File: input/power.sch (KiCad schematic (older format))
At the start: 59 parts, among them Q2 2STD1665T4, Q3 NSS1C300ET4G, U4 OPA830, U6 OPA830, U7 MCP1755S-3302E/DB, U8 NCP1117STAT3G

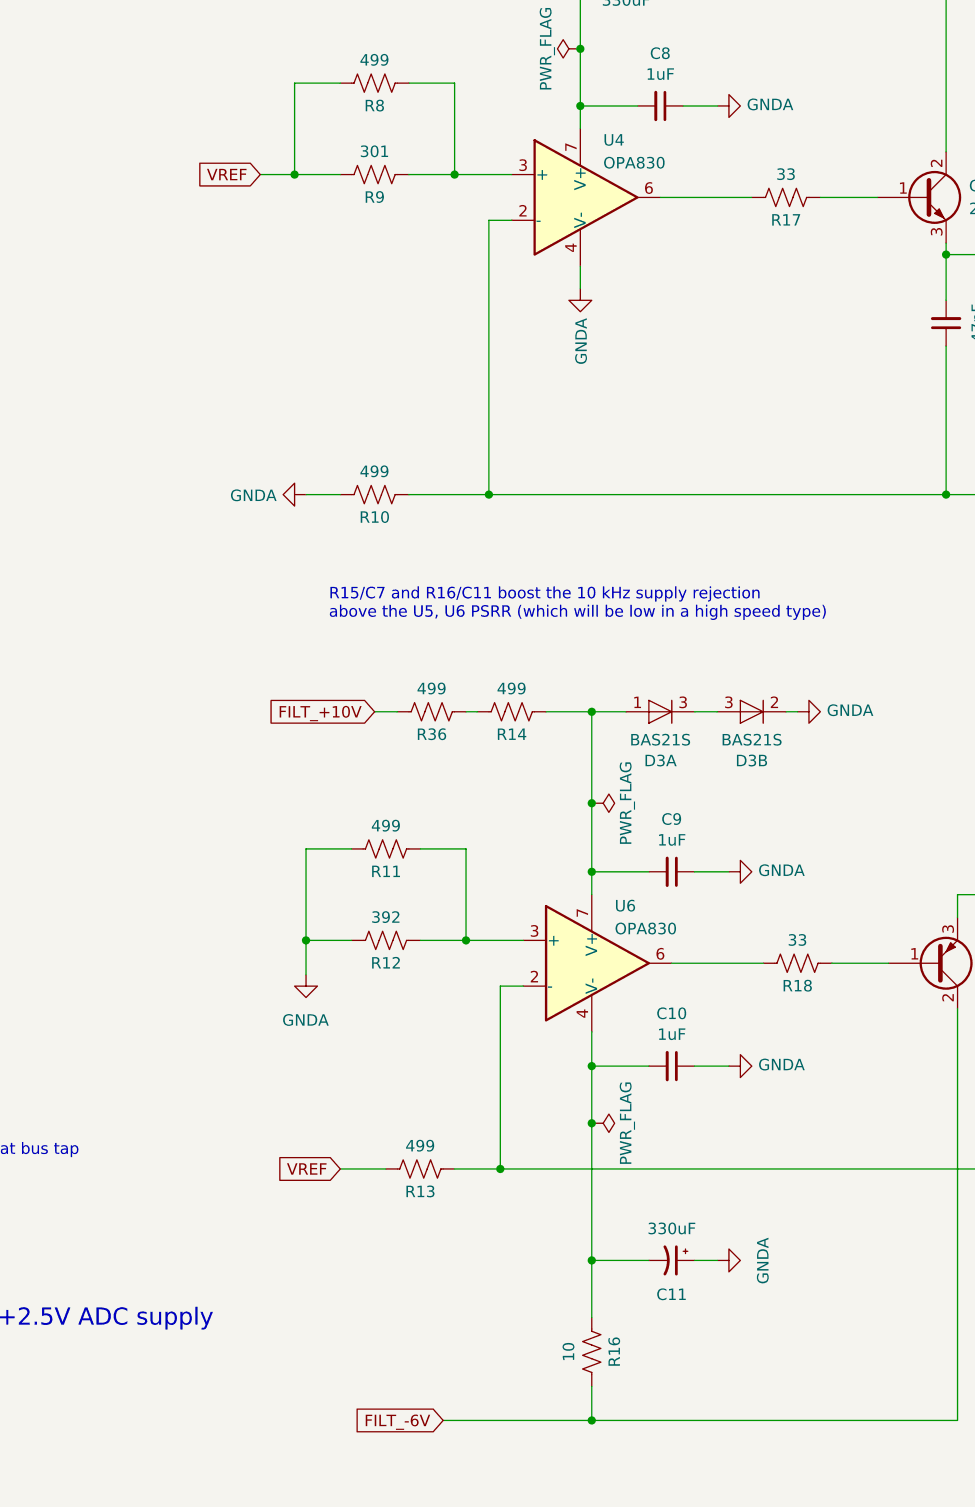
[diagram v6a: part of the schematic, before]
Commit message: Minor tweaks to schematic, and ongoing progress on PCB layout.
Changed BIST buffer to run off of CHAN1_V+, not the global V+.  This caused the CHAN_V+ net name to change.
On power.sch, added bypass caps for the VREF inputs to the V+/V- regulators.  Also, the BIST input lines now
have an RC filter, not just a resistor.
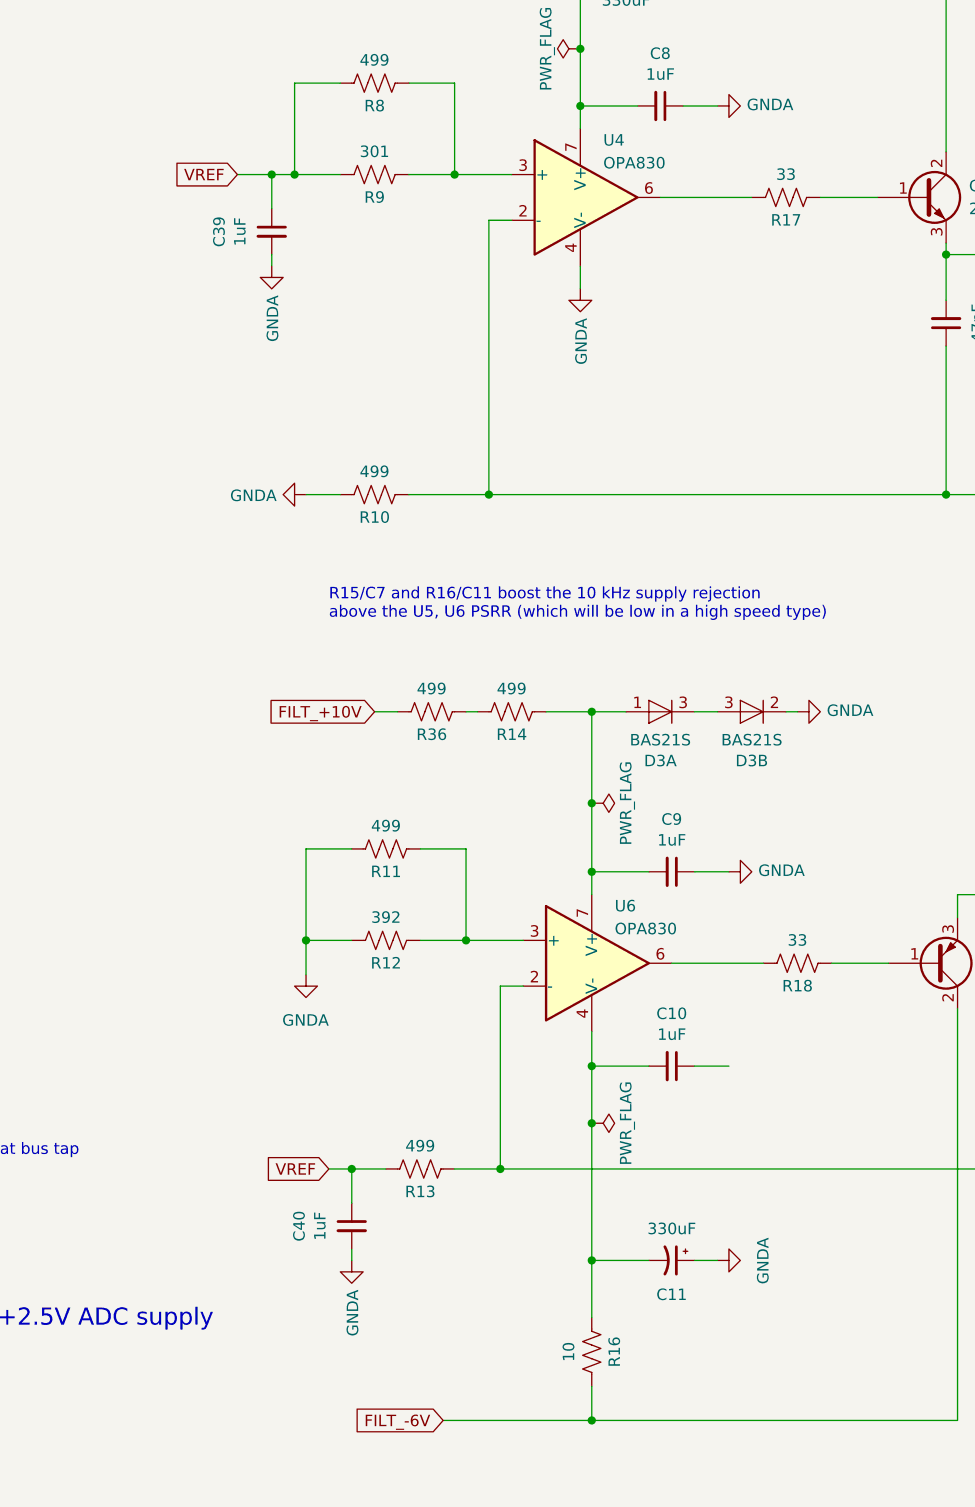
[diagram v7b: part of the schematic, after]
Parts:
- added C39, C40: 1uF, Capacitor_SMD:C_0805_2012Metric, symbol Device:C_Small
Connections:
- net GND: now also C39.2, C40.2; no longer C10.1
- net VREF: now also C39.1, C40.1
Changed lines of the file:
@@
 	0    -1   -1   0
 $EndComp
-Text GLabel 7200 2100 0    50   Input ~ 0
+Text GLabel 7100 2100 0    50   Input ~ 0
 VREF
 $Comp
@@
 	8050 6450 8250 6450
 Wire Wire Line
-	7550 6450 7750 6450
-Text GLabel 7550 6450 0    50   Input ~ 0
+	7500 6450 7600 6450
+Text GLabel 7500 6450 0    50   Input ~ 0
 VREF
 $Comp
@@
 L power:GNDA #PWR?
 U 1 1 5E52A14D
-P 9250 6000
+P 7600 6850
 AR Path="/5DFF6C0D/5E52A14D" Ref="#PWR?"  Part="1"
 AR Path="/5E1D6729/5E1DA2AA/5E52A14D" Ref="#PWR?"  Part="1"
 AR Path="/5E2EB92B/5E52A14D" Ref="#PWR?"  Part="1"
 AR Path="/5E51E83D/5E52A14D" Ref="#PWR029"  Part="1"
-F 0 "#PWR029" H 9250 5750 50  0001 C CNN
-F 1 "GNDA" V 9255 5872 50  0000 R CNN
-F 2 "" H 9250 6000 50  0001 C CNN
-F 3 "" H 9250 6000 50  0001 C CNN
-	1    9250 6000
-	0    -1   -1   0
+F 0 "#PWR029" H 7600 6600 50  0001 C CNN
+F 1 "GNDA" V 7605 6722 50  0000 R CNN
+F 2 "" H 7600 6850 50  0001 C CNN
+F 3 "" H 7600 6850 50  0001 C CNN
+	1    7600 6850
+	1    0    0    -1
 $EndComp
 $Comp
@@
 Connection ~ 8050 2100
 Wire Wire Line
-	7200 2100 7350 2100
+	7100 2100 7250 2100
 $Comp
 L Device:R_US R?
@@
 Wire Wire Line
 	7700 4450 7800 4450
+$Comp
+L Device:C_Small C?
+U 1 1 5E3DBA02
+P 7600 6700
+AR Path="/5DFF6C0D/5E3DBA02" Ref="C?"  Part="1"
+AR Path="/5E1D6729/5E1DA2AA/5E3DBA02" Ref="C?"  Part="1"
+AR Path="/5E2EB92B/5E3DBA02" Ref="C?"  Part="1"
+AR Path="/5E51E83D/5E3DBA02" Ref="C40"  Part="1"
+F 0 "C40" V 7371 6700 50  0000 C CNN
+F 1 "1uF" V 7462 6700 50  0000 C CNN
+F 2 "Capacitor_SMD:C_0805_2012Metric" H 7600 6700 50  0001 C CNN
+F 3 "https://media.digikey.com/pdf/Data%20Sheets/Samsung%20PDFs/CL_Series_MLCC_ds.pdf" H 7600 6700 50  0001 C CNN
+F 4 "CAP CER 1UF 16V X7R 0805 " H 7600 6700 50  0001 C CNN "Description"
+F 5 "1276-6471-1-ND" H 7600 6700 50  0001 C CNN "Digikey"
+F 6 "CL21B105KOFNNNG" H 7600 6700 50  0001 C CNN "MPN"
+F 7 "27" H 7600 6700 50  0001 C CNN "DK line"
+	1    7600 6700
+	1    0    0    -1
+$EndComp
+Wire Wire Line
+	7600 6600 7600 6450
+Connection ~ 7600 6450
+Wire Wire Line
+	7600 6450 7750 6450
+Wire Wire Line
+	7600 6800 7600 6850
+$Comp
+L power:GNDA #PWR?
+U 1 1 5E3F0E4B
+P 7250 2500
+AR Path="/5DFF6C0D/5E3F0E4B" Ref="#PWR?"  Part="1"
+AR Path="/5E1D6729/5E1DA2AA/5E3F0E4B" Ref="#PWR?"  Part="1"
+AR Path="/5E2EB92B/5E3F0E4B" Ref="#PWR?"  Part="1"
+AR Path="/5E51E83D/5E3F0E4B" Ref="#PWR0165"  Part="1"
+F 0 "#PWR0165" H 7250 2250 50  0001 C CNN
+F 1 "GNDA" V 7255 2372 50  0000 R CNN
+F 2 "" H 7250 2500 50  0001 C CNN
+F 3 "" H 7250 2500 50  0001 C CNN
+	1    7250 2500
+	1    0    0    -1
+$EndComp
+$Comp
+L Device:C_Small C?
+U 1 1 5E3F0E55
+P 7250 2350
+AR Path="/5DFF6C0D/5E3F0E55" Ref="C?"  Part="1"
+AR Path="/5E1D6729/5E1DA2AA/5E3F0E55" Ref="C?"  Part="1"
+AR Path="/5E2EB92B/5E3F0E55" Ref="C?"  Part="1"
+AR Path="/5E51E83D/5E3F0E55" Ref="C39"  Part="1"
+F 0 "C39" V 7021 2350 50  0000 C CNN
+F 1 "1uF" V 7112 2350 50  0000 C CNN
+F 2 "Capacitor_SMD:C_0805_2012Metric" H 7250 2350 50  0001 C CNN
+F 3 "https://media.digikey.com/pdf/Data%20Sheets/Samsung%20PDFs/CL_Series_MLCC_ds.pdf" H 7250 2350 50  0001 C CNN
+F 4 "CAP CER 1UF 16V X7R 0805 " H 7250 2350 50  0001 C CNN "Description"
+F 5 "1276-6471-1-ND" H 7250 2350 50  0001 C CNN "Digikey"
+F 6 "CL21B105KOFNNNG" H 7250 2350 50  0001 C CNN "MPN"
+F 7 "27" H 7250 2350 50  0001 C CNN "DK line"
+	1    7250 2350
+	1    0    0    -1
+$EndComp
+Wire Wire Line
+	7250 2450 7250 2500
+Wire Wire Line
+	7250 2250 7250 2100
+Connection ~ 7250 2100
+Wire Wire Line
+	7250 2100 7350 2100
 $EndSCHEMATC
